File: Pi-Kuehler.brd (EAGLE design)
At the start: 35.2 x 53.3 mm, 17 parts, among them IC1 MCP2515-I/SO, IC2 MCP2562-E/SN, Q1 16MHz, X1 RASPI_GPIO_B+#_PIN

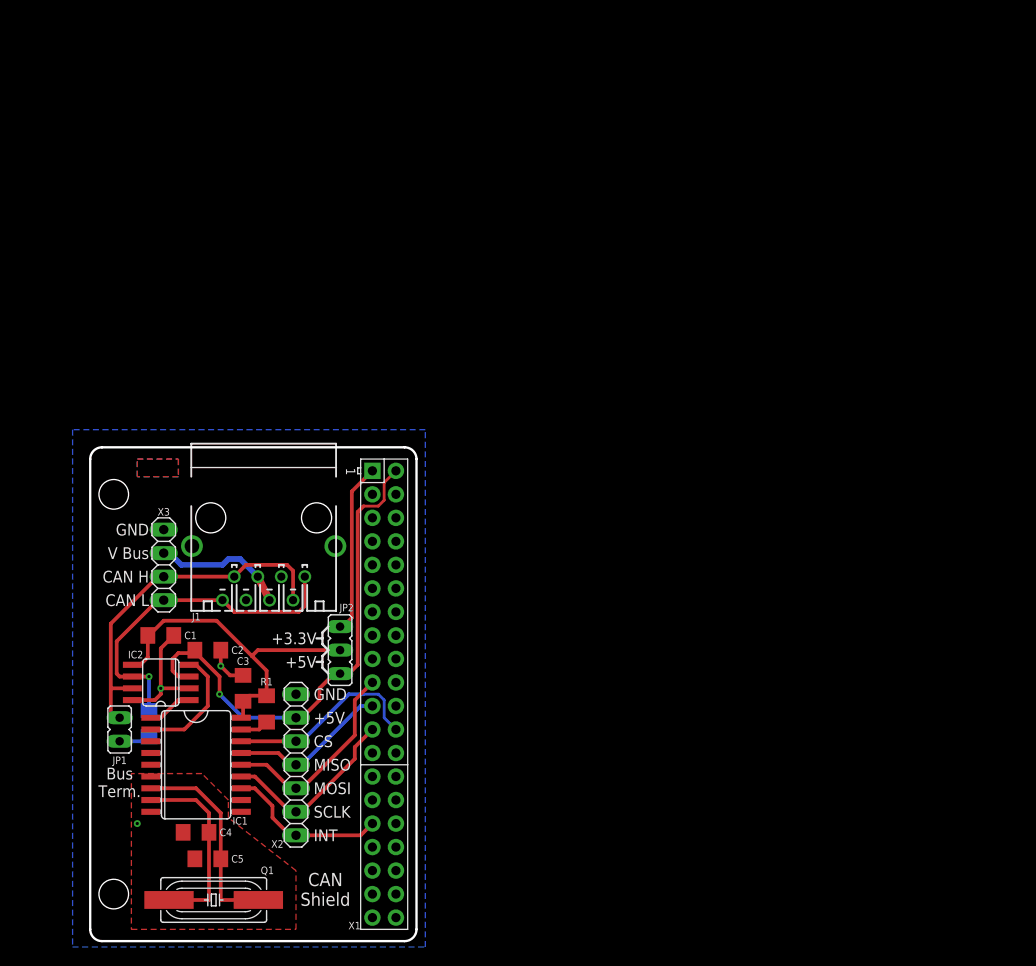
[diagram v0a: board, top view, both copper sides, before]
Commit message: Verbesserte Stromversorgung, Pi-Kühler, CAN-Bus 8x-Schalter
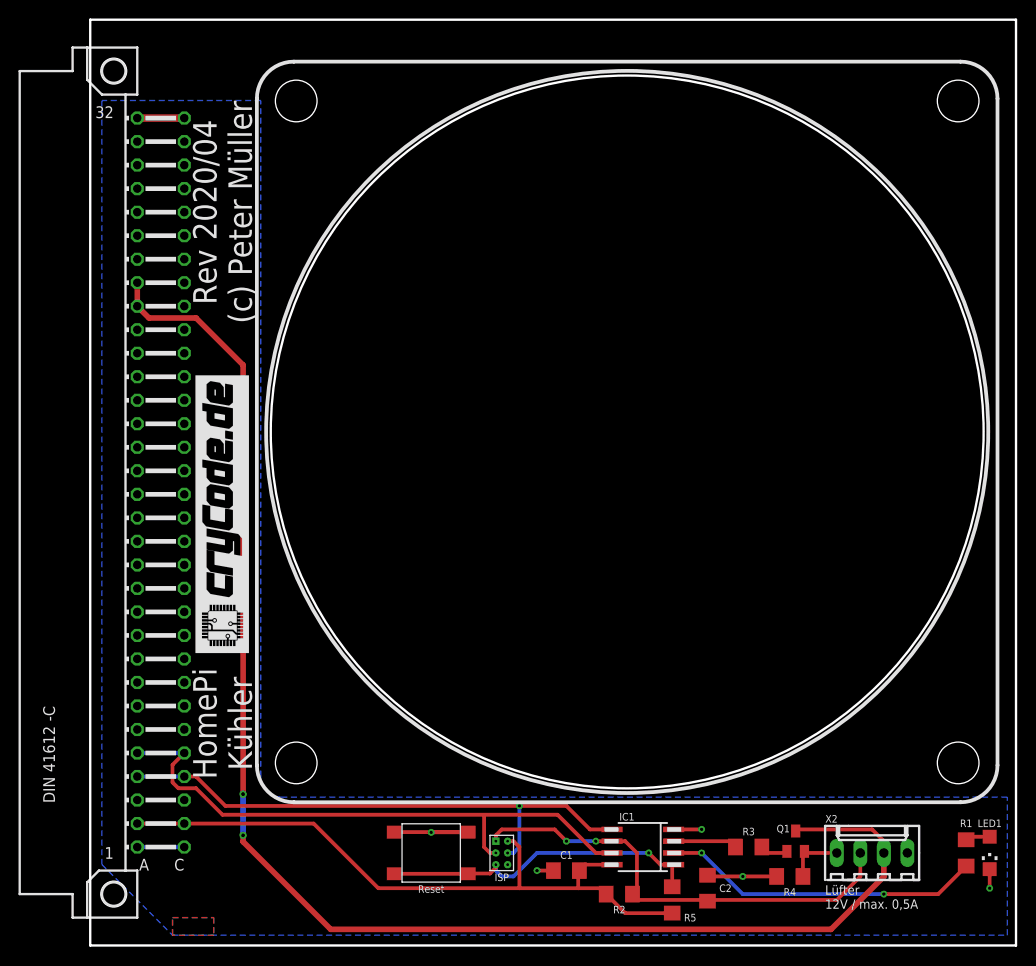
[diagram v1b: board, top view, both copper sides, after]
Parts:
- removed C3: 100nF, rcl:C1206
- removed C4, C5: 22pF, rcl:C1206
- removed IC2: MCP2562-E/SN, mcp2515_2551_2562:SO08
- removed J1: (no value), can-bus:MEBP_8-8G
- removed JP1: (no value), jumper:JP1
- removed JP2: (no value), jumper:JP2
- removed X3: (no value), pinhead:1X04
- added ISP: ISPVIAS-ONLY-1.27MM, pogo-isp:ISP-VIAS-ONLY-1.27MM
- added LED1: 2mA bl, led:CHIPLED_1206
- added R3, R4: 4k7, rcl:R1206
- added R5: 10k, rcl:R1206
- added S1: B3FS-1000, b3fs-1000:B3FS-1000
- added U$2: (no value), fan:80MM
- C2: value 100nF -> 1nF
- IC1: value MCP2515-I/SO -> ATTINY85-20S; device mcp2515_2551_2562:SO18L -> attiny25_45_85:SOIC8_EIAJ_208MIL
- Q1: value 16MHz -> BC847ASMD; device crystal:HC49UP -> transistor-npn:SOT23
- R1: value 4k7 -> 330
- R2: value 120R -> 4k7
- X1: value RASPI_GPIO_B+#_PIN -> MAC64L; device raspberrypi_bastelstube_v13:RASPI_GPIO_B+_PIN -> con-vg:MAC64L
- X2: value (none) -> FAN; device pinhead:1X07 -> con-molex:6410-04
- moved R1 77.1 mm to (94.6, 9.53)
- moved Q1 63.2 mm to (76.2, 10.8), turned to 0 degrees
- moved X2 63.0 mm to (84.5, 9.53), turned to 0 degrees
- moved C2 59.8 mm to (66.7, 5.71), turned to 90 degrees
- moved R2 54.0 mm to (57.1, 5.08), flipped to the top, turned to 180 degrees
- moved C1 50.6 mm to (51.4, 7.62), turned to 180 degrees
- moved IC1 49.1 mm to (59.7, 10.2), turned to 90 degrees
- moved X1 37.1 mm to (2.54, 49.5), turned to 180 degrees
- moved U$1 3.24 mm to (17.1, 31.1), flipped to the top, turned to 90 degrees
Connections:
- removed net +5V: C2.1, IC2.3, JP2.3, X1.2, X2.2
- removed net 3V3B: X1.17
- removed net 5V0B: X1.4
- removed net CANH: IC2.7, J1.2, J1.7, JP1.1, X3.3
- removed net CANL: IC2.6, J1.1, J1.8, R2.1, X3.4
- removed net GND_B: X1.9
- removed net GND_C: X1.14
- removed net GND_D: X1.20
- removed net GND_E: X1.25
- removed net GND_F: X1.30
- removed net GND_G: X1.34
- removed net GND_H: X1.39
- removed net MCP_VCC: C1.1, C3.1, IC1.18, IC2.5, JP2.2, R1.2
- removed net N$3: JP1.2, R2.2
- removed net N$4: C5.1, IC1.7, Q1.1
- removed net RXCAN: IC1.2, IC2.4
- removed net TXCAN: IC1.1, IC2.1
- new net !PI_RESET: X1.A26
- new net !RESET: IC1.1, ISP.RST, R5.1, S1.3, S1.4
- new net +12V: Q1.3, X1.A24, X1.A25, X2.2
- new net +5V_EXT: X1.C31
- new net +5V_INT: X1.A1, X1.C1
- new net +5V_INT2: X1.C28
- new net 1WIRE: X1.C7
- new net GND_EXT: X1.C30
- new net GPIO.05: X1.C14
- new net GPIO.12: X1.C16
- new net GPIO.13: X1.C17
- new net GPIO.16: X1.C18
- new net GPIO.17: X1.C19
- new net GPIO.18: X1.C20
- new net GPIO.19: X1.C21
- new net GPIO.20: X1.C22
- new net GPIO.21: X1.C23
- new net GPIO.22: X1.C24
- new net GPIO.23: X1.C25
- new net GPIO.24: X1.C26
- new net GPIO.25: X1.C27
- new net I2C_SCL: IC1.7, ISP.SCK, X1.A5, X1.C5
- new net I2C_SDA: IC1.5, ISP.MOSI, X1.A4, X1.C4
- new net LED: IC1.2, R1.1
- new net N$15: LED1.A, R1.2
- new net PI_RXD: X1.C12
- new net PI_TXD: X1.A12
- new net PWM: Q1.2, R4.2, X2.4
- new net SPI_CE1: X1.C11
- new net TACHO: C2.1, IC1.6, ISP.MISO, R2.1, X2.3
- net +24V: now also X1.A32, X1.C32; no longer J1.4, J1.5, X3.2
- net +3,3V: now also C1.1, IC1.8, ISP.VCC, R2.2, R5.2, X1.A2, X1.C2; no longer JP2.1, X1.1
- net GND: now also IC1.4, ISP.GND, LED1.C, R4.1, S1.1, S1.2, X1.A29, X1.A3, X1.A6, X1.A8, X1.C29, X1.C3, X1.C6, X1.C8; no longer C3.2, C4.2, C5.2, IC1.9, IC2.2, IC2.8, J1.3, J1.6, J1.G1, J1.G2, X1.6, X3.1
- net GPIO.06: now also X1.C15; no longer IC1.12, X1.31, X2.7
- net N$1: now also IC1.3, R3.1; no longer C4.1, IC1.8, Q1.2
- net N$2: now also Q1.1, R3.2; no longer IC1.17, R1.1
- net SPI_CE0: now also X1.A10; no longer IC1.16, X1.24, X2.3
- net SPI_MISO: now also X1.A9; no longer IC1.15, X1.21, X2.4
- net SPI_MOSI: now also X1.C9; no longer IC1.14, X1.19, X2.5
- net SPI_SCLK: now also X1.C10; no longer IC1.13, X1.23, X2.6
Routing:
- net +12V: track 0.00 -> 157.5 mm, vias 0 -> 2
- net I2C_SCL: track 0.00 -> 64.4 mm
- net I2C_SDA: track 0.00 -> 59.6 mm, vias 0 -> 1
- net +3,3V: track 18.5 -> 73.5 mm
- net +5V: track 54.6 -> 0.00 mm, vias 1 -> 0
- net TACHO: track 0.00 -> 50.5 mm, vias 0 -> 2
- net CANH: track 39.0 -> 0.00 mm
- net MCP_VCC: track 37.2 -> 0.00 mm
- net CANL: track 36.9 -> 0.00 mm, vias 1 -> 0
- net !RESET: track 0.00 -> 35.7 mm, vias 0 -> 1
- net LED: track 0.00 -> 34.7 mm, vias 0 -> 2
- net SPI_MOSI: track 22.2 -> 0.00 mm
- net N$4: track 22.1 -> 0.00 mm
- net SPI_CE0: track 21.5 -> 0.00 mm
- net SPI_SCLK: track 20.2 -> 0.00 mm
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- removed copper zone on layer 16, net BOT
- removed copper zone on layer 1, net GND
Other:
- board size 35.2 x 53.3 mm -> 100 x 100 mm
- board text added: "HomePi Kühler"
- board text added: "Lüfter 12V / max. 0,5A"
- board text added: "Reset"
- board text added: "Rev 2020/04 (c) Peter Müller"
- board text removed: "+3.3V"
- board text removed: "+5V"
- board text removed: "Bus Term."
- board text removed: "CAN H"
- board text removed: "CAN L"
- board text removed: "CAN Shield"
- board text removed: "CS"
- board text removed: "GND"
- board text removed: "HomePi CAN-Bus"
- board text removed: "INT"
- board text removed: "MISO"
- board text removed: "MOSI"
- board text removed: "Raspbarry Pi / Universal CAN-Shield Rev. 2020/04 (C) 2020 Peter Müller <peter@crycode.de>"
- board text removed: "SCLK"
- board text removed: "V Bus"
- board text removed: "V+"

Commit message: Schaltpläne optimiert
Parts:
- R1: value 330 -> 1k2
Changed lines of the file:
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@@
 </autorouter>
 <elements>
-<element name="R1" library="rcl" package="R1206" value="330" x="94.615" y="9.525" smashed="yes" rot="R90">
+<element name="R1" library="rcl" package="R1206" value="1k2" x="94.615" y="9.525" smashed="yes" rot="R90">
 <attribute name="NAME" x="94.615" y="12.319" size="0.8128" layer="25" font="vector" rot="R180" align="top-center"/>
 <attribute name="VALUE" x="97.155" y="8.255" size="1.27" layer="27" rot="R90"/>
